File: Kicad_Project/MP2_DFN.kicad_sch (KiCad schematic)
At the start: 236 parts, among them J1 Conn_01x07, J2 Conn_01x06, J3 Conn_01x06, J4 Conn_01x06, U1 TF2190-TAH, U2 TF2190-TAH, U3 TF2190-TAH, U4 NCS20034DR2G, U5 STM32F405_pill, U6 PQDE6W-Q110 / RD5-110S12W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

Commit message: using JLC plugin to manage rotations
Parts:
- C19, C4: value 3.3nF -> 22nF; LCSC C1613 -> C21122
- CS1, CS2, CS3, NTC1, RS1, RS2, RS3: now not fitted
- RN1, RN2, RN3, RN4, RN5, RN7, U4: JLCPCB Rotation Offset (none) -> 90
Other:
- note added: "22 to 33nF appropriate for a ~2khz filter"

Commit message: changes from MP2 v0.6 i think it is now, readded some parts to the pcb, and fixed some minor tidyness thingies
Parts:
- removed C4: 22nF, Capacitor_SMD:C_0603_1608Metric, symbol Device:C
- removed D7: SMBJ85A, Diode_SMD:D_SMB, symbol Diode:SM6T75A
- removed R4: 11k, Resistor_SMD:R_0603_1608Metric, symbol Device:R
- removed R40: 13k, Resistor_SMD:R_0603_1608Metric, symbol Device:R
- C5: LCSC C28233 -> C342865; MFR PT CL21B104KCFNNNE -> C2012X7T2E104KT000N
- CD1, CD2, CD3, CD4, CD5, CD6, CX1, CX2, CX20, CX3, CX4, CX5, CX6, CX7, CX8, CX9: value 4.7uF -> 470nF; LCSC C381466 -> C192761; MFR PT FS32X475K101EGG -> FM32X474K251EGG
- D8: value SMCJ85A -> ~; MFR PT SMBJ85A -> (none); now not fitted
- QA1: footprint NVMTSC4D3N15MC:custom_NVMTSC4D3N15MC -> MP2_DFN_Custom_parts:custom_NVMTSC4D3N15MC; now in the parts list
- R14: value 270k -> 360k; LCSC C17589 -> C17645; MFR PT 0805W8F2703T5E -> 0805W8F3603T5E
- R15: value 11k -> 8k2; LCSC C25950 -> C25981; MFR PT 0603WAF1102T5E -> 0603WAF8201T5E
- R17: value 8k2 -> 22k; LCSC C25981 -> C31850; MFR PT 0603WAF8201T5E -> 0603WAF2202T5E
- R3: value 270k -> 100k; footprint Resistor_SMD:R_0805_2012Metric -> Resistor_SMD:R_0603_1608Metric; LCSC C17589 -> C25803; MFR PT 0805W8F2703T5E -> 0603WAF1003T5E
- R38: value 13k -> 220k; LCSC C22797 -> C22961; MFR PT 0603WAF4702T5E -> 0603WAF2203T5E
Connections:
- net GND: now also R3.2
- net VBAT: no longer R3.2
- net VSENSE2: no longer names the net of D4.1 (K), D5.1 (K), D6.1 (K), R3.1, U4.13 (-)
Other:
- note added: "values for Vsense dividers - -> ratio is exactly the same as 3.3k and 150k of the phase sense dividers, so this can be used as the only values in software for a more foolproof software setup. (0.18% error) -> i did not use 3.3k and 150k to lower the off-state current draw of the esc."
- note removed: "R38 and R40 values for Vsense dividers - for different power stage Voltages. Since the we're going with the NVMTSC4D3N15MC MOSFETs, Vsense will be for 150V: 150V max 30s lipo, overvoltage cutoff at 137V) - 13k (LCSC C22797) 100V max 20s lipo, overvoltage cutoff at 92.6V) - 47k (LCSC C25819) 80V max 16s lipo, overvoltage cutoff at 75.6V) - Do not fit at all!"

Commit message: V0.2 JLCPCB order 12/26/23
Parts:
- QA2, QA3, QA4, QA5, QA6, QB1, QB2, QB3, QB4, QB5, QB6, QC1, QC2, QC3, QC4, QC5, QC6: now in the parts list
- SHA1, SHA2, SHA3, SHB1, SHB2, SHB3, SHC1, SHC2, SHC3: LCSC C500733 -> C710260
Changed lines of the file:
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@@
   )
   (symbol (lib_id "MP2_DFN_Custom_Symbols:MDP10N027") (at 496.57 63.5 0) (unit 1)
-    (in_bom no) (on_board yes) (dnp no)
+    (in_bom yes) (on_board yes) (dnp no)
     (property "Reference" "QA3" (at 508 67.3099 0)
       (effects (font (size 1.27 1.27)) (justify left))
@@
   )
   (symbol (lib_id "MP2_DFN_Custom_Symbols:MDP10N027") (at 527.05 143.51 0) (unit 1)
-    (in_bom no) (on_board yes) (dnp no)
+    (in_bom yes) (on_board yes) (dnp no)
     (property "Reference" "QB5" (at 538.48 147.3199 0)
       (effects (font (size 1.27 1.27)) (justify left))
@@
   )
   (symbol (lib_id "MP2_DFN_Custom_Symbols:MDP10N027") (at 467.36 143.51 0) (unit 1)
-    (in_bom no) (on_board yes) (dnp no)
+    (in_bom yes) (on_board yes) (dnp no)
     (property "Reference" "QB1" (at 478.79 147.3199 0)
       (effects (font (size 1.27 1.27)) (justify left))
@@
   )
   (symbol (lib_id "MP2_DFN_Custom_Symbols:MDP10N027") (at 467.36 83.82 0) (unit 1)
-    (in_bom no) (on_board yes) (dnp no)
+    (in_bom yes) (on_board yes) (dnp no)
     (property "Reference" "QA2" (at 478.79 87.6299 0)
       (effects (font (size 1.27 1.27)) (justify left))
@@
       (effects (font (size 1.27 1.27)) hide)
     )
-    (property "LCSC" "C500733" (at 474.98 185.42 0)
+    (property "LCSC" "C710260" (at 474.98 185.42 0)
       (effects (font (size 1.27 1.27)) hide)
     )
@@
   )
   (symbol (lib_id "MP2_DFN_Custom_Symbols:MDP10N027") (at 496.57 163.83 0) (unit 1)
-    (in_bom no) (on_board yes) (dnp no)
+    (in_bom yes) (on_board yes) (dnp no)
     (property "Reference" "QB4" (at 508 167.6399 0)
       (effects (font (size 1.27 1.27)) (justify left))
@@
   )
   (symbol (lib_id "MP2_DFN_Custom_Symbols:MDP10N027") (at 527.05 245.11 0) (unit 1)
-    (in_bom no) (on_board yes) (dnp no)
+    (in_bom yes) (on_board yes) (dnp no)
     (property "Reference" "QC6" (at 537.21 247.015 0)
       (effects (font (size 1.27 1.27)) (justify left))
@@
       (effects (font (size 1.27 1.27)) hide)
     )
-    (property "LCSC" "C500733" (at 534.67 266.7 0)
+    (property "LCSC" "C710260" (at 534.67 266.7 0)
       (effects (font (size 1.27 1.27)) hide)
     )
@@
   )
   (symbol (lib_id "MP2_DFN_Custom_Symbols:MDP10N027") (at 467.36 224.79 0) (unit 1)
-    (in_bom no) (on_board yes) (dnp no)
+    (in_bom yes) (on_board yes) (dnp no)
     (property "Reference" "QC1" (at 476.885 226.06 0)
       (effects (font (size 1.27 1.27)) (justify left))
@@
   )
   (symbol (lib_id "MP2_DFN_Custom_Symbols:MDP10N027") (at 527.05 224.79 0) (unit 1)
-    (in_bom no) (on_board yes) (dnp no)
+    (in_bom yes) (on_board yes) (dnp no)
     (property "Reference" "QC5" (at 537.21 228.6 0)
       (effects (font (size 1.27 1.27)) (justify left))
@@
   )
   (symbol (lib_id "MP2_DFN_Custom_Symbols:MDP10N027") (at 496.57 143.51 0) (unit 1)
-    (in_bom no) (on_board yes) (dnp no)
+    (in_bom yes) (on_board yes) (dnp no)
     (property "Reference" "QB3" (at 508 147.3199 0)
       (effects (font (size 1.27 1.27)) (justify left))
@@
   )
   (symbol (lib_id "MP2_DFN_Custom_Symbols:MDP10N027") (at 496.57 224.79 0) (unit 1)
-    (in_bom no) (on_board yes) (dnp no)
+    (in_bom yes) (on_board yes) (dnp no)
     (property "Reference" "QC3" (at 506.73 226.695 0)
       (effects (font (size 1.27 1.27)) (justify left))
@@
       (effects (font (size 1.27 1.27)) hide)
     )
-    (property "LCSC" "C500733" (at 474.98 266.7 0)
+    (property "LCSC" "C710260" (at 474.98 266.7 0)
       (effects (font (size 1.27 1.27)) hide)
     )
@@
       (effects (font (size 1.27 1.27)) hide)
     )
-    (property "LCSC" "C500733" (at 534.67 185.42 0)
+    (property "LCSC" "C710260" (at 534.67 185.42 0)
       (effects (font (size 1.27 1.27)) hide)
     )
@@
   )
   (symbol (lib_id "MP2_DFN_Custom_Symbols:MDP10N027") (at 496.57 245.11 0) (unit 1)
-    (in_bom no) (on_board yes) (dnp no)
+    (in_bom yes) (on_board yes) (dnp no)
     (property "Reference" "QC4" (at 506.73 247.65 0)
       (effects (font (size 1.27 1.27)) (justify left))
@@
       (effects (font (size 1.27 1.27)) hide)
     )
-    (property "LCSC" "C500733" (at 474.98 105.41 0)
+    (property "LCSC" "C710260" (at 474.98 105.41 0)
       (effects (font (size 1.27 1.27)) hide)
     )
@@
   )
   (symbol (lib_id "MP2_DFN_Custom_Symbols:MDP10N027") (at 527.05 63.5 0) (unit 1)
-    (in_bom no) (on_board yes) (dnp no)
+    (in_bom yes) (on_board yes) (dnp no)
     (property "Reference" "QA5" (at 538.48 67.3099 0)
       (effects (font (size 1.27 1.27)) (justify left))
@@
       (effects (font (size 1.27 1.27)) hide)
     )
-    (property "LCSC" "C500733" (at 504.19 185.42 0)
+    (property "LCSC" "C710260" (at 504.19 185.42 0)
       (effects (font (size 1.27 1.27)) hide)
     )
@@
       (effects (font (size 1.27 1.27)) hide)
     )
-    (property "LCSC" "C500733" (at 534.67 105.41 0)
+    (property "LCSC" "C710260" (at 534.67 105.41 0)
       (effects (font (size 1.27 1.27)) hide)
     )
@@
       (effects (font (size 1.27 1.27)) hide)
     )
-    (property "LCSC" "C500733" (at 504.19 105.41 0)
+    (property "LCSC" "C710260" (at 504.19 105.41 0)
       (effects (font (size 1.27 1.27)) hide)
     )
@@
       (effects (font (size 1.27 1.27)) hide)
     )
-    (property "LCSC" "C500733" (at 504.19 266.7 0)
+    (property "LCSC" "C710260" (at 504.19 266.7 0)
       (effects (font (size 1.27 1.27)) hide)
     )
@@
   )
   (symbol (lib_id "MP2_DFN_Custom_Symbols:MDP10N027") (at 527.05 83.82 0) (unit 1)
-    (in_bom no) (on_board yes) (dnp no)
+    (in_bom yes) (on_board yes) (dnp no)
     (property "Reference" "QA6" (at 538.48 87.6299 0)
       (effects (font (size 1.27 1.27)) (justify left))
@@
   )
   (symbol (lib_id "MP2_DFN_Custom_Symbols:MDP10N027") (at 467.36 245.11 0) (unit 1)
-    (in_bom no) (on_board yes) (dnp no)
+    (in_bom yes) (on_board yes) (dnp no)
     (property "Reference" "QC2" (at 476.885 246.38 0)
       (effects (font (size 1.27 1.27)) (justify left))
@@
   )
   (symbol (lib_id "MP2_DFN_Custom_Symbols:MDP10N027") (at 467.36 163.83 0) (unit 1)
-    (in_bom no) (on_board yes) (dnp no)
+    (in_bom yes) (on_board yes) (dnp no)
     (property "Reference" "QB2" (at 478.79 167.6399 0)
       (effects (font (size 1.27 1.27)) (justify left))
@@
   )
   (symbol (lib_id "MP2_DFN_Custom_Symbols:MDP10N027") (at 496.57 83.82 0) (unit 1)
-    (in_bom no) (on_board yes) (dnp no)
+    (in_bom yes) (on_board yes) (dnp no)
     (property "Reference" "QA4" (at 508 87.6299 0)
       (effects (font (size 1.27 1.27)) (justify left))
@@
   )
   (symbol (lib_id "MP2_DFN_Custom_Symbols:MDP10N027") (at 527.05 163.83 0) (unit 1)
-    (in_bom no) (on_board yes) (dnp no)
+    (in_bom yes) (on_board yes) (dnp no)
     (property "Reference" "QB6" (at 538.48 167.6399 0)
       (effects (font (size 1.27 1.27)) (justify left))

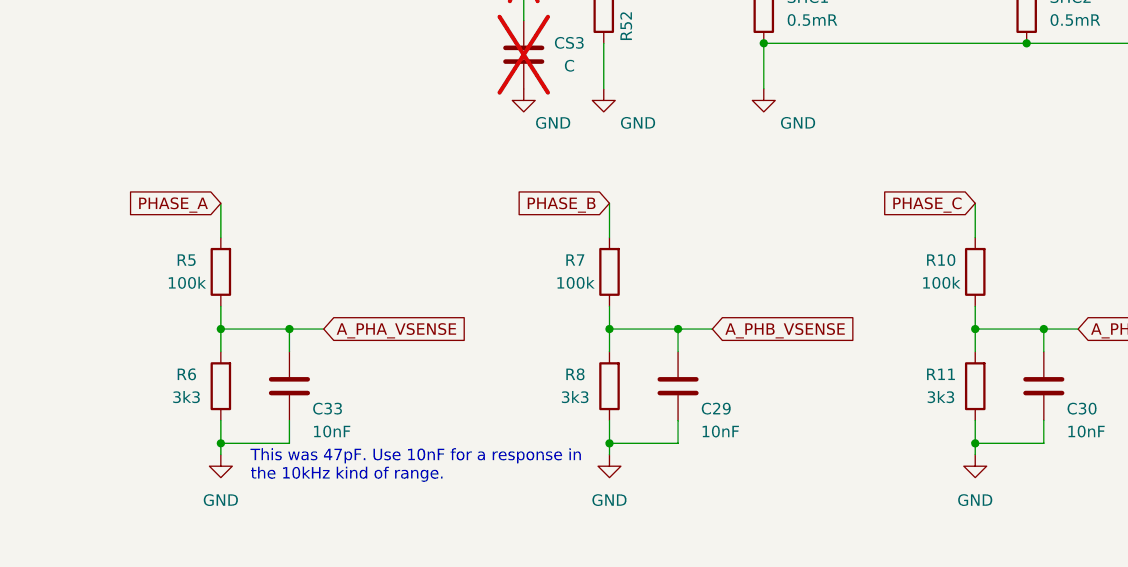
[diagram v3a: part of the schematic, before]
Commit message: changed phase voltage sense dividers to 150-3.3 - as it should hav beeen
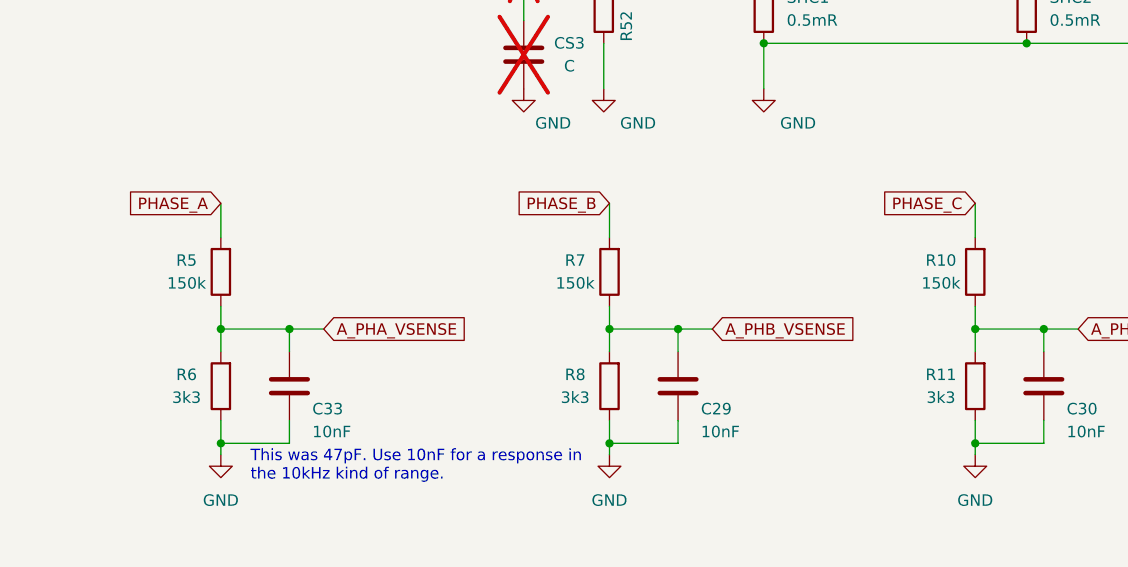
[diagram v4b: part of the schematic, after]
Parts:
- R10, R5, R7: value 100k -> 150k; LCSC C149504 -> C17470; MFR PT 0805W8F1003T5E -> 0805W8F1503T5E
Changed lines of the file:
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@@
       (effects (font (size 1.27 1.27)))
     )
-    (property "Value" "100k" (at 454.025 297.18 0)
+    (property "Value" "150k" (at 454.025 297.18 0)
       (effects (font (size 1.27 1.27)))
     )
@@
       (effects (font (size 1.27 1.27)) hide)
     )
-    (property "MFR PT" "0805W8F1003T5E" (at 457.835 295.91 0)
+    (property "MFR PT" "0805W8F1503T5E" (at 457.835 295.91 0)
       (effects (font (size 1.27 1.27)) hide)
     )
-    (property "LCSC" "C149504" (at 457.835 295.91 0)
+    (property "LCSC" "C17470" (at 457.835 295.91 0)
       (effects (font (size 1.27 1.27)) hide)
     )
@@
       (effects (font (size 1.27 1.27)))
     )
-    (property "Value" "100k" (at 410.845 297.18 0)
+    (property "Value" "150k" (at 410.845 297.18 0)
       (effects (font (size 1.27 1.27)))
     )
@@
       (effects (font (size 1.27 1.27)) hide)
     )
-    (property "MFR PT" "0805W8F1003T5E" (at 414.655 295.91 0)
+    (property "MFR PT" "0805W8F1503T5E" (at 414.655 295.91 0)
       (effects (font (size 1.27 1.27)) hide)
     )
-    (property "LCSC" "C149504" (at 414.655 295.91 0)
+    (property "LCSC" "C17470" (at 414.655 295.91 0)
       (effects (font (size 1.27 1.27)) hide)
     )
@@
       (effects (font (size 1.27 1.27)))
     )
-    (property "Value" "100k" (at 494.665 297.18 0)
+    (property "Value" "150k" (at 494.665 297.18 0)
       (effects (font (size 1.27 1.27)))
     )
@@
       (effects (font (size 1.27 1.27)) hide)
     )
-    (property "MFR PT" "0805W8F1003T5E" (at 498.475 295.91 0)
+    (property "MFR PT" "0805W8F1503T5E" (at 498.475 295.91 0)
       (effects (font (size 1.27 1.27)) hide)
     )
-    (property "LCSC" "C149504" (at 498.475 295.91 0)
+    (property "LCSC" "C17470" (at 498.475 295.91 0)
       (effects (font (size 1.27 1.27)) hide)
     )

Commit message: wip
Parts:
- removed CGS11, CGS12, CGS14, CGS15, CGS17, CGS18: 4.7nF, Capacitor_SMD:C_0603_1608Metric, symbol Device:C_Small
- removed CGS2, CGS3, CGS5, CGS6, CGS8, CGS9: 4.7nF, Capacitor_SMD:C_0603_1608Metric, symbol Device:C
- removed CR1, CR2, CR3, CR4, CR5: 470uF, Capacitor_THT:CP_Radial_D18.0mm_P7.50mm, symbol Device:C_Polarized
- removed CX1, CX2, CX20, CX3, CX4, CX5, CX6, CX7, CX8, CX9: 470nF, Capacitor_SMD:C_1210_3225Metric, symbol Device:C
- removed PHA_2, PHB_2, PHC_2: PhasePad, TestPoint:my_2mm_slot, symbol Connector:TestPoint
- removed QA3, QA4, QA5, QA6, QB3, QB4, QB5, QB6, QC3, QC4, QC5, QC6: NVMTSC4D3N15MC, NVMTSC4D3N15MC:custom_NVMTSC4D3N15MC, symbol MP2_DFN_Custom_Symbols:MDP10N027
- removed RG11, RG12, RG14, RG15, RG17, RG18, RG2, RG3, RG5, RG6, RG8, RG9: 15R, Resistor_SMD:R_0603_1608Metric, symbol Device:R
- removed SHA2, SHA3, SHB2, SHB3, SHC2, SHC3: 0.5mR, MP2_DFN_Custom_parts:Shunt_2512_6332Metric, symbol Device:R
- removed TpGND1, TpGND2, TpGND3, TpGND5, TpGND6, TpGND7, TpVBAT1, TpVBAT2, TpVBAT3, TpVBAT4, TpVBAT5: TestPoint, Busbars:my_testpoint_D1.7mm, symbol Connector:TestPoint
- removed TpGND4: TestPoint, TestPoint:TestPoint_THTPad_D3.0mm_Drill1.5mm, symbol Connector:TestPoint
- added C35, C36, C37, C4: C, Capacitor_THT:C_Rect_L27.0mm_W11.0mm_P22.00mm, symbol Device:C
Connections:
- net GND: now also C35.2, C36.2, C37.2, C4.2
- net VBAT: now also C35.1, C36.1, C37.1, C4.1
